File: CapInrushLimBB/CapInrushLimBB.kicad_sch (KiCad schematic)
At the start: 28 parts, among them J2 Screw_Terminal_01x02, J3 Screw_Terminal_01x02, K1 G5LE-1, Q1 IRF9540N, Q2 Q_PMOS_GDSD, Q3 MPSA42, Q4 MPSA42

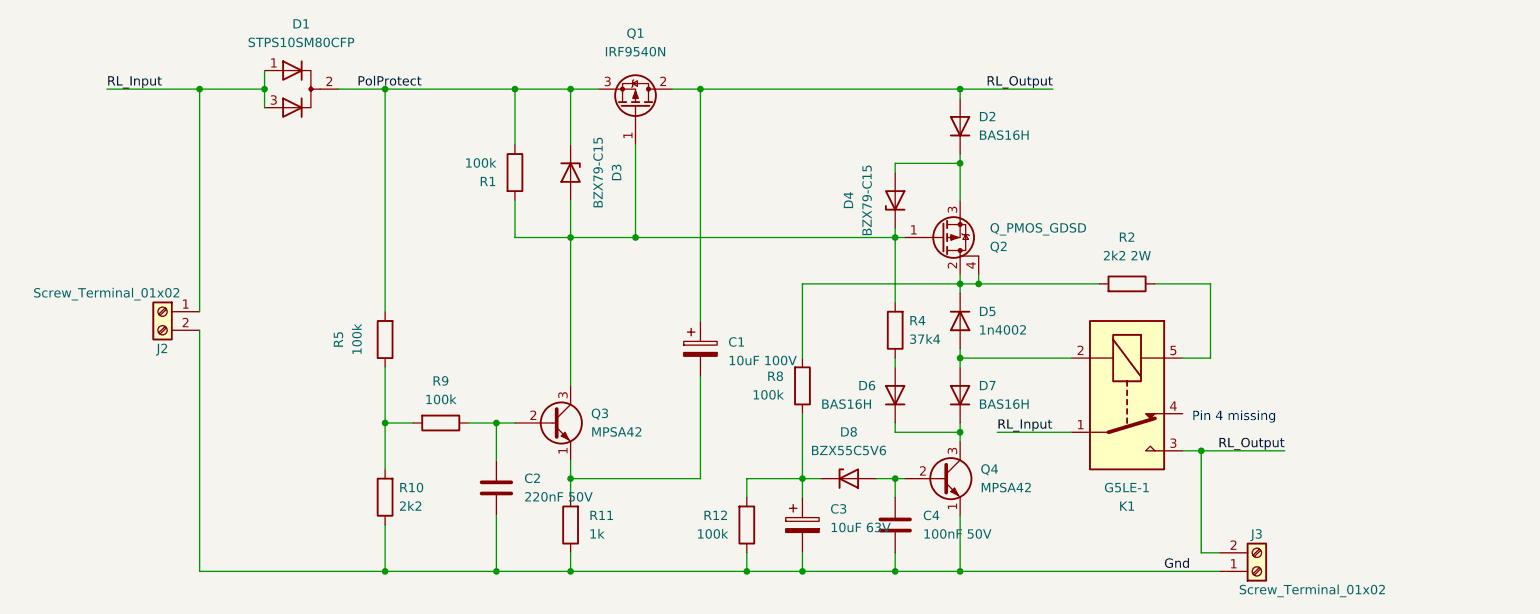
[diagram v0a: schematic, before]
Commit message: Updated model and schematic values.
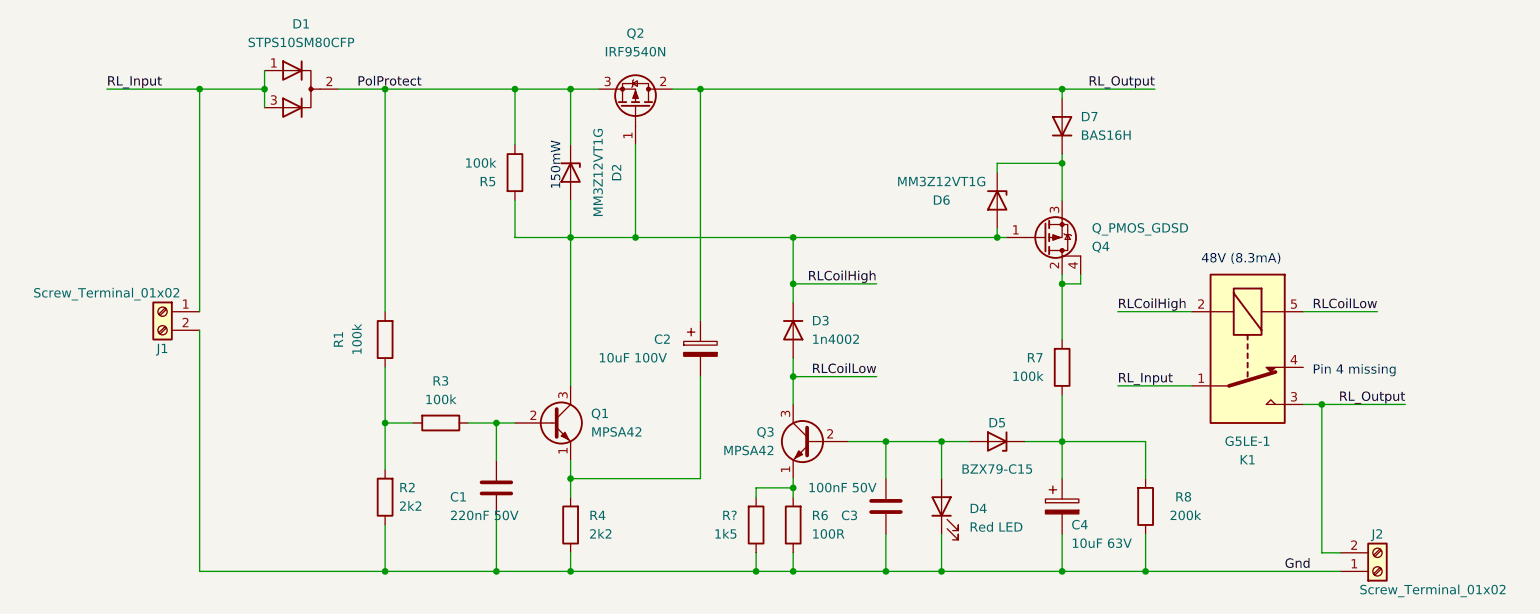
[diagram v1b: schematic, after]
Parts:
- removed D6, D7: BAS16H, Diode_SMD:D_SOD-323_HandSoldering, symbol Device:D
- removed D8: BZX55C5V6, Diode_THT:D_DO-35_SOD27_P7.62mm_Horizontal, symbol Device:D_Zener
- removed R2: 2k2 2W, Resistor_THT:R_Axial_DIN0414_L11.9mm_D4.5mm_P20.32mm_Horizontal, symbol Device:R
- removed R4: 37k4, Resistor_THT:R_Axial_DIN0207_L6.3mm_D2.5mm_P7.62mm_Horizontal, symbol Device:R
- added D4: Red LED, symbol Device:LED
- added D6: MM3Z12VT1G, Diode_THT:D_DO-35_SOD27_P7.62mm_Horizontal, symbol Device:D_Zener
- added R6: 100R, Resistor_THT:R_Axial_DIN0207_L6.3mm_D2.5mm_P7.62mm_Horizontal, symbol Device:R
- added R?: 1k5, Resistor_THT:R_Axial_DIN0207_L6.3mm_D2.5mm_P7.62mm_Horizontal, symbol Device:R
- D2: renamed from D3; value BZX79-C15 -> MM3Z12VT1G
- R4: renamed from R11; value 1k -> 2k2
- R8: renamed from R12; value 100k -> 200k
- renumbered C2 to C1, C1 to C2, C4 to C3, C3 to C4, D5 to D3, D4 to D5, D2 to D7, J2 to J1, J3 to J2, Q3 to Q1, Q1 to Q2, Q4 to Q3, Q2 to Q4, R5 to R1, R10 to R2, R9 to R3, R1 to R5, R8 to R7
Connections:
- net Gnd: now also C3.1, D4.1 (K), R6.1, R?.1; no longer C3.2, Q3.1 (E)
- net RLCoilHigh: now reaches D2.2 (A), Q1.3 (C), Q2.1 (G), Q4.1 (G), R5.2
- net RLCoilHigh: now also D3.1 (K), K1.2, D6.2 (A); no longer D5.1 (K)
- net at C4.1, R7.1, R8.2: now also D5.1 (K)
- net at Q4.2 (D), Q4.4 (D), R7.2: no longer D3.1 (K)
- net RLCoilLow: now reaches D3.2 (A)
- net RLCoilLow: now also K1.5, Q3.3 (C); no longer K1.2
- net at D7.1 (K), Q4.3 (S): now also D6.1 (K); no longer D5.2 (A)
- net at Q3.2 (B): now also C3.2, D5.2 (A), D4.2 (A); no longer C3.1
- new net: Q3.1 (E), R6.2, R?.2
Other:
- note added: "150mW"
- note added: "48V (8.3mA)"
- moved on the sheet: C3, C4, D3, D5, D7, J2, K1, Q3, Q4, R7, R8

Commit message: Updated values and footprints.
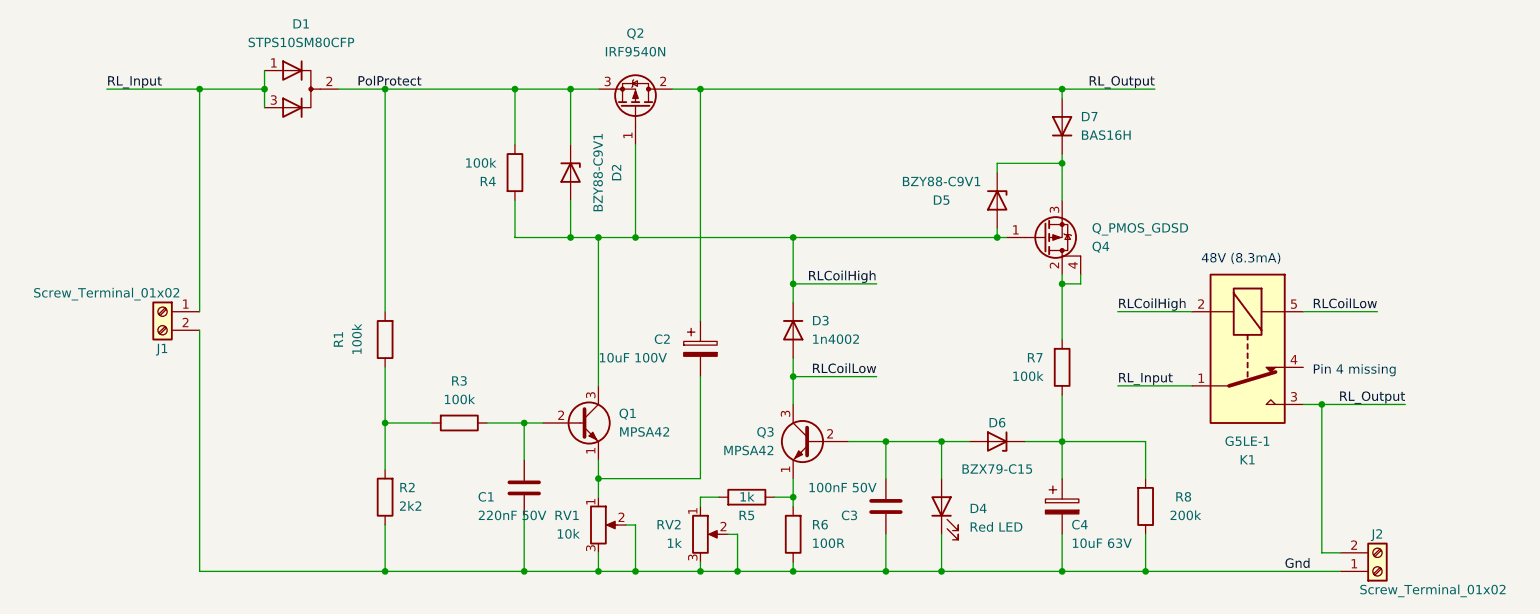
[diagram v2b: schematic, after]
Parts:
- removed R4: 2k2, Resistor_THT:R_Axial_DIN0207_L6.3mm_D2.5mm_P7.62mm_Horizontal, symbol Device:R
- added RV1: 10k, Potentiometer_THT:Potentiometer_Bourns_3296W_Vertical, symbol Device:R_Potentiometer
- added RV2: 1k, Potentiometer_THT:Potentiometer_Bourns_3296W_Vertical, symbol Device:R_Potentiometer
- D2: value MM3Z12VT1G -> BZY88-C9V1
- D4: footprint (none) -> LED_THT:LED_D5.0mm
- D5: renamed from D6; value MM3Z12VT1G -> BZY88-C9V1
- R5: renamed from R?; value 1k5 -> 1k
- renumbered D5 to D6, R5 to R4
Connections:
- net Gnd: now also RV1.2, RV1.3, RV2.2, RV2.3; no longer R5.1
- net at Q3.1 (E), R6.2: now also R5.1; no longer R5.2
- net at C2.2, Q1.1 (E): now also RV1.1
- new net: R5.2, RV2.1
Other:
- note removed: "150mW"
- moved on the sheet: C1, Q1, R3, R5, R6

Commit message: First layout complete
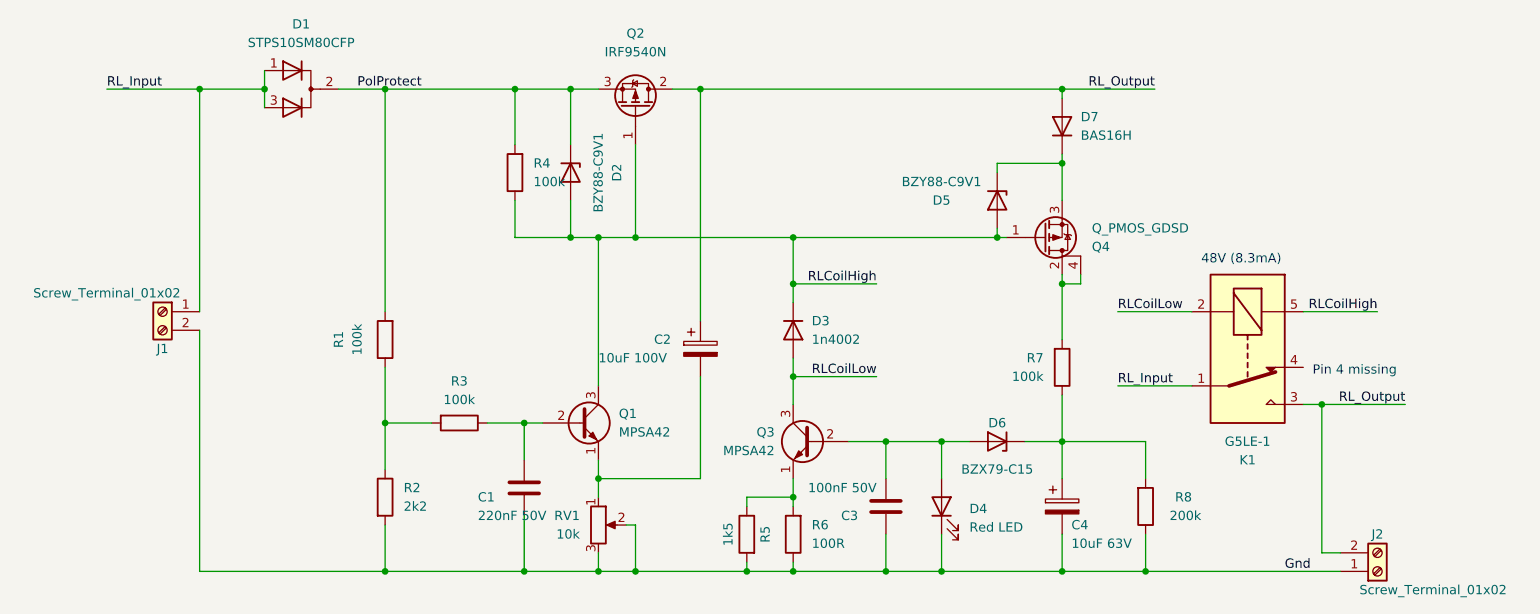
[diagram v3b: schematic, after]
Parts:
- removed RV2: 1k, Potentiometer_THT:Potentiometer_Bourns_3296W_Vertical, symbol Device:R_Potentiometer
- D2: footprint Diode_THT:D_DO-35_SOD27_P7.62mm_Horizontal -> Diode_THT:D_DO-35_SOD27_P5.08mm_Vertical_AnodeUp
- D3: footprint Diode_THT:D_DO-41_SOD81_P10.16mm_Horizontal -> Diode_THT:D_DO-41_SOD81_P2.54mm_Vertical_KathodeUp
- D5, D6: footprint Diode_THT:D_DO-35_SOD27_P7.62mm_Horizontal -> Diode_THT:D_DO-35_SOD27_P2.54mm_Vertical_AnodeUp
- R1, R2, R3, R4, R6, R7, R8: footprint Resistor_THT:R_Axial_DIN0207_L6.3mm_D2.5mm_P7.62mm_Horizontal -> Resistor_THT:R_Axial_DIN0207_L6.3mm_D2.5mm_P2.54mm_Vertical
- R5: value 1k -> 1k5; footprint Resistor_THT:R_Axial_DIN0207_L6.3mm_D2.5mm_P7.62mm_Horizontal -> Resistor_THT:R_Axial_DIN0207_L6.3mm_D2.5mm_P2.54mm_Vertical
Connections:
- net Gnd: now also R2.2, R5.2; no longer R2.1
- net PolProtect: now also R4.2; no longer R4.1
- net RLCoilHigh: now also K1.5, R4.1; no longer K1.2, R4.2
- net RLCoilLow: now also K1.2; no longer K1.5
- net at R1.1, R3.2: now also R2.1; no longer R2.2
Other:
- moved on the sheet: R2, R4, R5

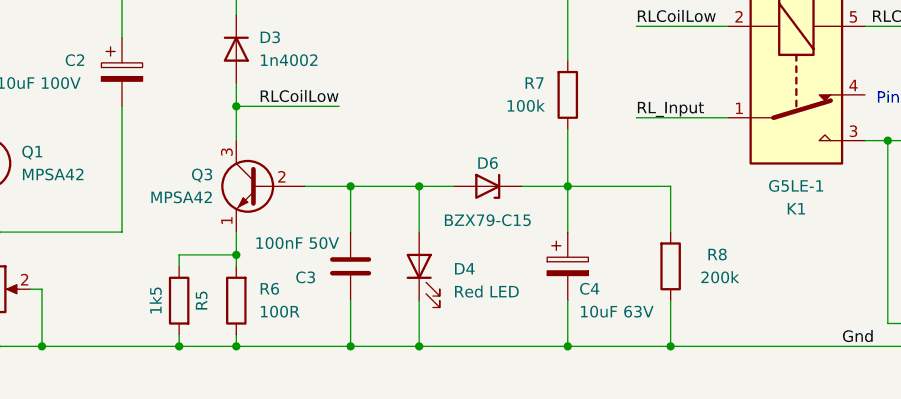
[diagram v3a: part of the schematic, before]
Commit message: Tweaked some component orientations to give space for through board connections.
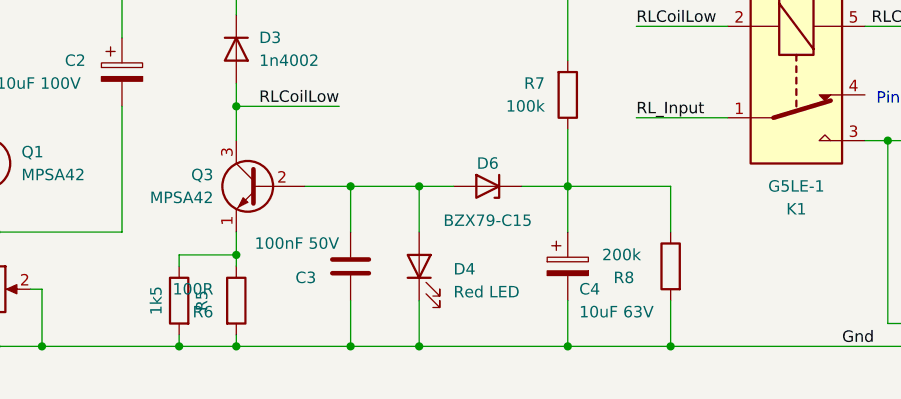
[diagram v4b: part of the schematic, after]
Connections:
- net Gnd: now also R6.2, R8.2; no longer R6.1, R8.1
- net at Q3.1 (E), R5.1: now also R6.1; no longer R6.2
- net at C4.1, D6.1 (K), R7.1: now also R8.1; no longer R8.2
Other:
- moved on the sheet: R6
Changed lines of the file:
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@@
     (effects (font (size 1.27 1.27)) (justify right bottom))
   )
-  (symbol (lib_id "Device:R") (at 124.46 134.62 180) (unit 1)
-    (in_bom yes) (on_board yes)
-    (property "Reference" "R6" (id 0) (at 127 133.3499 0)
-      (effects (font (size 1.27 1.27)) (justify right))
-    )
-    (property "Value" "100R" (id 1) (at 127 135.8899 0)
-      (effects (font (size 1.27 1.27)) (justify right))
-    )
-    (property "Footprint" "Resistor_THT:R_Axial_DIN0207_L6.3mm_D2.5mm_P2.54mm_Vertical" (id 2) (at 126.238 134.62 90)
+  (symbol (lib_id "Device:R") (at 124.46 134.62 0) (unit 1)
+    (in_bom yes) (on_board yes)
+    (property "Reference" "R6" (id 0) (at 121.92 135.8901 0)
+      (effects (font (size 1.27 1.27)) (justify right))
+    )
+    (property "Value" "100R" (id 1) (at 121.92 133.3501 0)
+      (effects (font (size 1.27 1.27)) (justify right))
+    )
+    (property "Footprint" "Resistor_THT:R_Axial_DIN0207_L6.3mm_D2.5mm_P2.54mm_Vertical" (id 2) (at 122.682 134.62 90)
       (effects (font (size 1.27 1.27)) hide)
     )
@@
     (pin "2")
   )
-  (symbol (lib_id "Device:R") (at 172.72 130.81 0) (mirror x) (unit 1)
-    (in_bom yes) (on_board yes)
-    (property "Reference" "R8" (id 0) (at 179.07 129.54 0)
-      (effects (font (size 1.27 1.27)) (justify right))
-    )
-    (property "Value" "200k" (id 1) (at 180.34 132.08 0)
-      (effects (font (size 1.27 1.27)) (justify right))
-    )
-    (property "Footprint" "Resistor_THT:R_Axial_DIN0207_L6.3mm_D2.5mm_P2.54mm_Vertical" (id 2) (at 170.942 130.81 90)
-      (effects (font (size 1.27 1.27)) hide)
-    )
+  (symbol (lib_id "Device:R") (at 172.72 130.81 0) (mirror y) (unit 1)
+    (in_bom yes) (on_board yes)
+    (property "Reference" "R8" (id 0) (at 166.37 132.08 0)
+      (effects (font (size 1.27 1.27)) (justify right))
+    )
+    (property "Value" "200k" (id 1) (at 165.1 129.54 0)
+      (effects (font (size 1.27 1.27)) (justify right))
+    )
+    (property "Footprint" "Resistor_THT:R_Axial_DIN0207_L6.3mm_D2.5mm_P2.54mm_Vertical" (id 2) (at 174.498 130.81 90)
+      (effects (font (size 1.27 1.27)) hide)
+    )

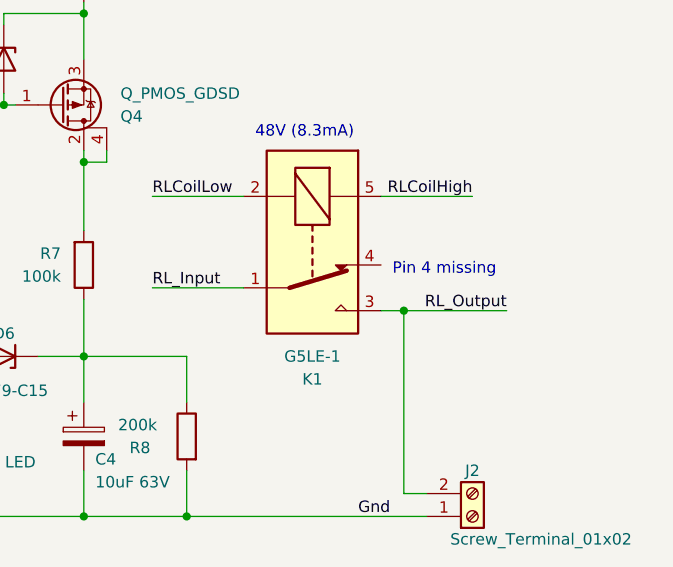
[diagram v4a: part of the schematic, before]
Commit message: Updated relay footprint and tweaked track layout so it rounds nicley.
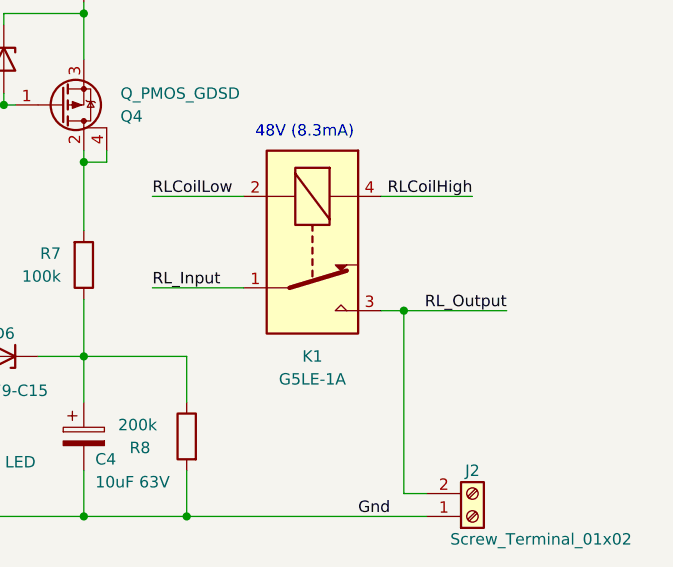
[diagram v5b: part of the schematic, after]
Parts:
- removed K1: G5LE-1, Relay_THT:Relay_SPDT_Omron-G5LE-1, symbol Relay:G5LE-1
- added K1: G5LE-1A, CapInrushLim:Relay_SPST-NO_Omron-G5LE-1A, symbol CapInrushLim:G5LE-1A
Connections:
- net RLCoilHigh: now also K1.4
- net RLCoilLow: now also K1.2
- net RL_Input: now also K1.1
- net RL_Output: now also K1.3
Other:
- note removed: "Pin 4 missing"
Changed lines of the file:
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@@
     (stroke (width 0) (type default) (color 0 0 0 0))
-  )
-  (text "Pin 4 missing" (at 195.58 113.03 0)
-    (effects (font (size 1.27 1.27)) (justify left bottom))
   )
   (text "48V (8.3mA)" (at 180.34 97.79 0)
@@
   (label "RLCoilLow" (at 135.89 113.03 180)
     (effects (font (size 1.27 1.27)) (justify right bottom))
+  )
+  (symbol (lib_id "CapInrushLim:G5LE-1A") (at 186.69 109.22 270) (unit 1)
+    (in_bom yes) (on_board yes)
+    (property "Reference" "K1" (id 0) (at 186.69 121.92 90))
+    (property "Value" "G5LE-1A" (id 1) (at 186.69 124.46 90))
+    (property "Footprint" "CapInrushLim:Relay_SPST-NO_Omron-G5LE-1A" (id 2) (at 185.42 120.65 0)
+      (effects (font (size 1.27 1.27)) (justify left) hide)
+    )
+    (property "Datasheet" "http://www.omron.com/ecb/products/pdf/en-g5le.pdf" (id 3) (at 186.69 109.22 0)
+      (effects (font (size 1.27 1.27)) hide)
+    )
+    (pin "1")
+    (pin "2")
+    (pin "3")
+    (pin "4")
   )
   (symbol (lib_id "Device:R") (at 124.46 134.62 0) (unit 1)
@@
     (pin "2")
   )
-  (symbol (lib_id "Relay:G5LE-1") (at 186.69 109.22 270) (unit 1)
-    (in_bom yes) (on_board yes)
-    (property "Reference" "K1" (id 0) (at 186.69 124.46 90))
-    (property "Value" "G5LE-1" (id 1) (at 186.69 121.92 90))
-    (property "Footprint" "Relay_THT:Relay_SPDT_Omron-G5LE-1" (id 2) (at 185.42 120.65 0)
-      (effects (font (size 1.27 1.27)) (justify left) hide)
-    )
-    (property "Datasheet" "http://www.omron.com/ecb/products/pdf/en-g5le.pdf" (id 3) (at 186.69 109.22 0)
-      (effects (font (size 1.27 1.27)) hide)
-    )
-    (pin "1")
-    (pin "2")
-    (pin "3")
-    (pin "4")
-    (pin "5")
-  )
   (symbol (lib_id "Device:R") (at 118.11 134.62 0) (mirror y) (unit 1)
     (in_bom yes) (on_board yes)
@@
       (reference "J2") (unit 1) (value "Screw_Terminal_01x02") (footprint "TerminalBlock:TerminalBlock_Altech_AK300-2_P5.00mm")
     )
-    (path "/31274493-5996-4b83-999c-5bc71df402ff"
-      (reference "K1") (unit 1) (value "G5LE-1") (footprint "Relay_THT:Relay_SPDT_Omron-G5LE-1")
+    (path "/03023a4d-5cf8-4e65-ad10-161a38e81293"
+      (reference "K1") (unit 1) (value "G5LE-1A") (footprint "CapInrushLim:Relay_SPST-NO_Omron-G5LE-1A")
     )
     (path "/a9f6f942-45df-4f12-8f1d-f9e51724c8de"
